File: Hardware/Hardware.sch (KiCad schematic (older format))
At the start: 13 parts

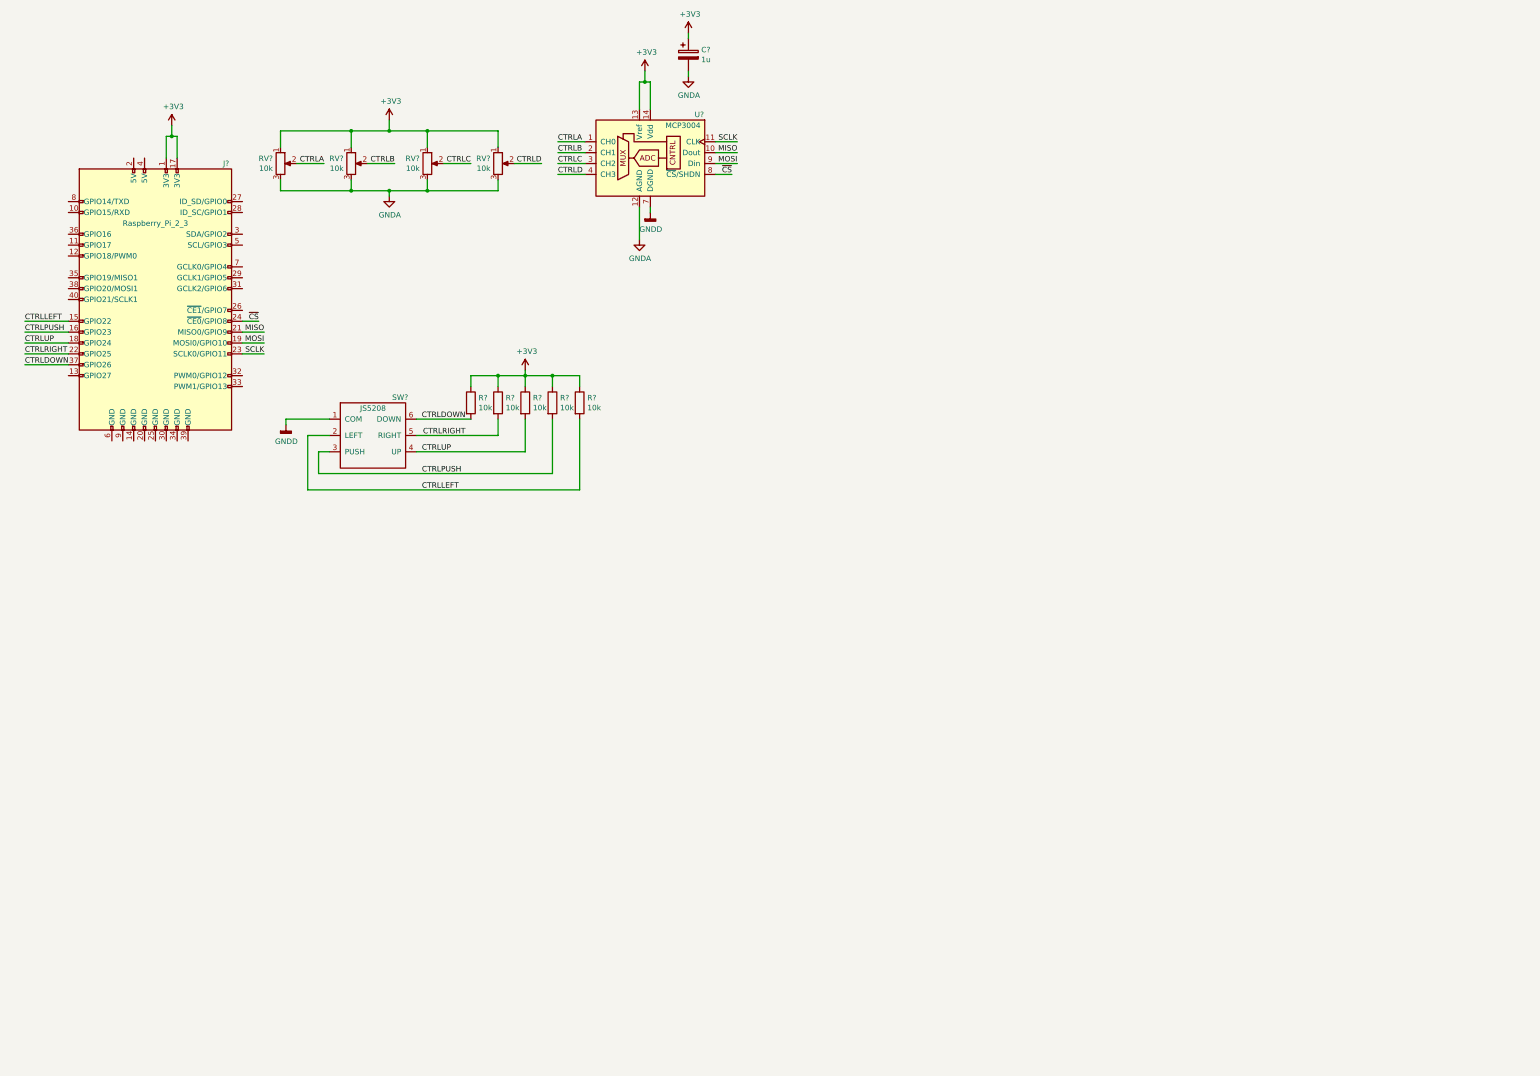
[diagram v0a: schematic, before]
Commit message: Added WM8731SEDS to schematic and connected all relevant external circuitry, modified WM8731SEDS schematic part to aid routing
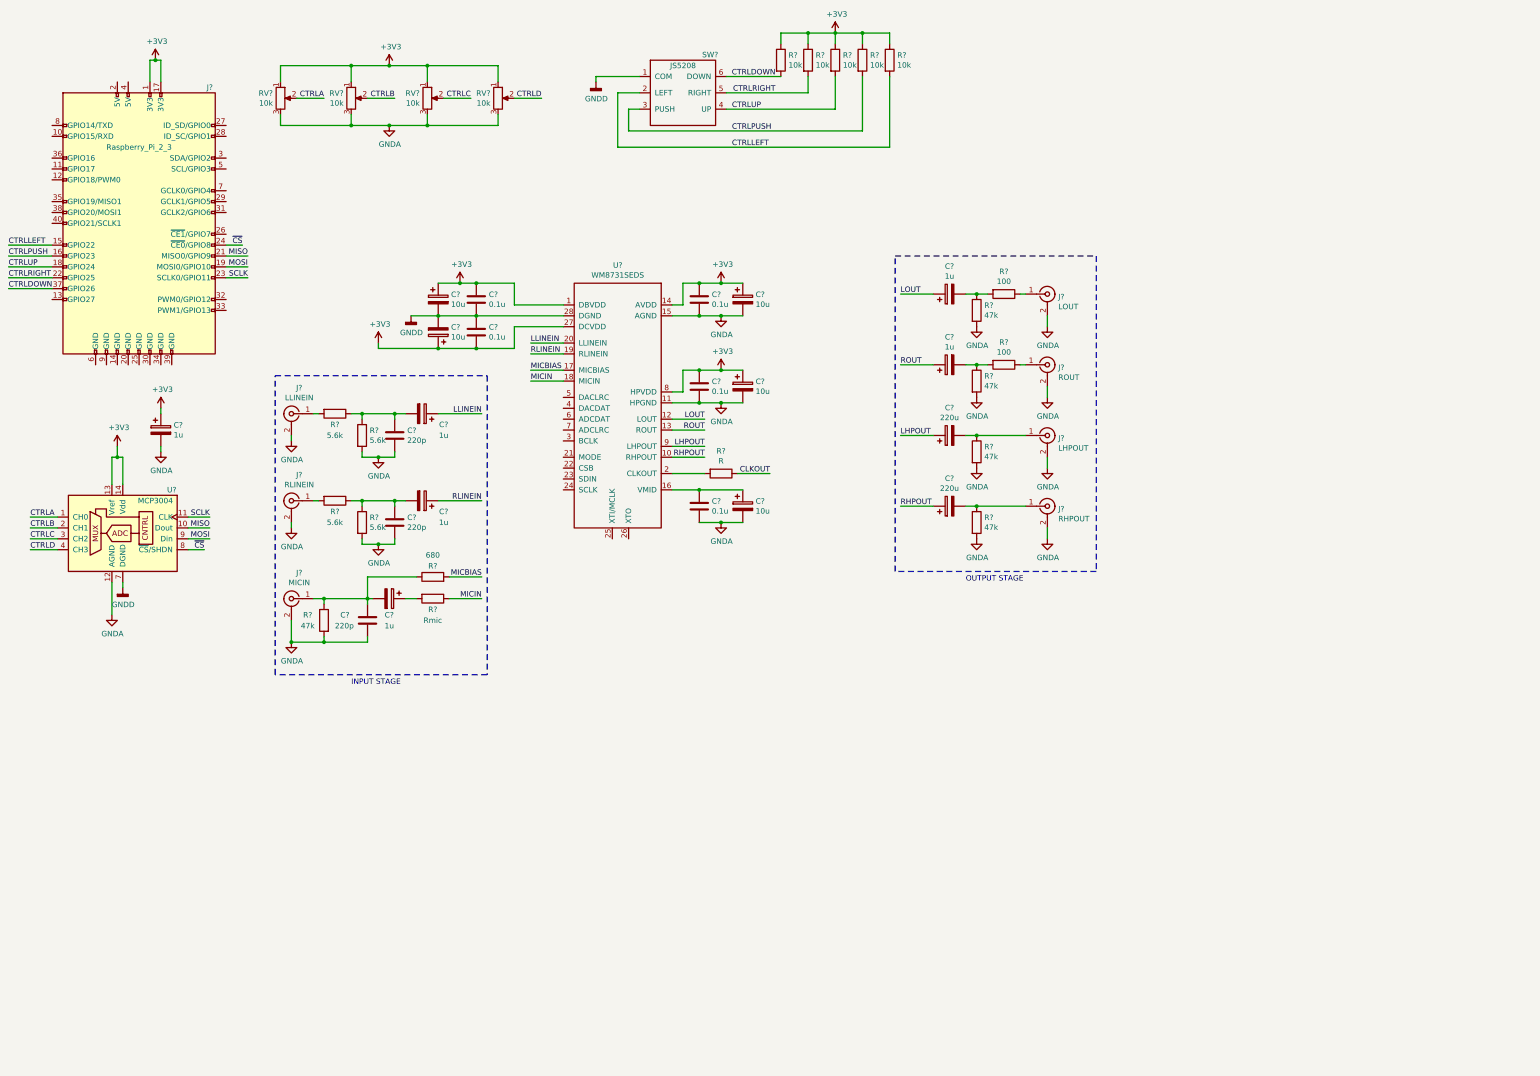
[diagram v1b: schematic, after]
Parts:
- added C? (x5): 0.1u, symbol Device:C
- added C? (x5): 10u, symbol Device:CP
- added C? (x5): 1u, symbol Device:CP
- added C? (x3): 220p, symbol Device:C
- added C? (x2): 220u, symbol Device:CP
- added J?: LLINEIN, symbol Connector:Conn_Coaxial
- added J?: RLINEIN, symbol Connector:Conn_Coaxial
- added J?: MICIN, symbol Connector:Conn_Coaxial
- added J?: LOUT, symbol Connector:Conn_Coaxial
- added J?: ROUT, symbol Connector:Conn_Coaxial
- added J?: LHPOUT, symbol Connector:Conn_Coaxial
- added J?: RHPOUT, symbol Connector:Conn_Coaxial
- added R? (x4): 5.6k, symbol Device:R
- added R?: 680, symbol Device:R
- added R?: Rmic, symbol Device:R
- added R? (x5): 47k, symbol Device:R
- added R? (x2): 100, symbol Device:R
- added R?: R, symbol Device:R
- added U?: WM8731SEDS, Package_SO:SSOP-28_5.3x10.2mm_P0.65mm, symbol signl:WM8731SEDS
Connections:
- net +3V3: now also C?.1, C?.1, C?.1, C?.1, C?.1, C?.1, C?.1, C?.2, U?.1 (DBVDD), U?.14 (AVDD), U?.27 (DCVDD), U?.8 (HPVDD)
- net GNDA: now also C?.2, C?.2, C?.2, C?.2, C?.2, C?.2, C?.2, C?.2, C?.2, J?.2 (Ext), J?.2 (Ext), J?.2 (Ext), J?.2 (Ext), J?.2 (Ext), J?.2 (Ext), J?.2 (Ext), R?.2, R?.2, R?.2, R?.2, R?.2, R?.2, R?.2, U?.11 (HPGND), U?.15 (AGND)
- net GNDD: now also C?.1, C?.2, C?.2, C?.2, U?.28 (DGND)
- new net: C?.1, C?.1, U?.16 (VMID)
- new net: R?.2, U?.2 (CLKOUT)
- new net: C?.1, C?.2, R?.1, R?.1 (x2)
- new net: J?.1 (In), R?.2 (x2)
- new net: C?.1, C?.2, J?.1 (In), R?.1, R?.1
- new net: C?.1, R?.2
- new net: C?.2, R?.1, R?.2 (x2)
- new net: J?.1 (In), R?.1 (x2)
- new net: C?.2, J?.1 (In), R?.1 (x2)
- new net CLKOUT: R?.1
- new net LHPOUT: C?.1, U?.9 (LHPOUT)
- new net LLINEIN: C?.1, U?.20 (LLINEIN)
- new net LOUT: C?.1, U?.12 (LOUT)
- new net MICBIAS: R?.2, U?.17 (MICBIAS)
- new net MICIN: R?.1, U?.18 (MICIN)
- new net RHPOUT: C?.1, U?.10 (RHPOUT)
- new net RLINEIN: C?.1, U?.19 (RLINEIN)
- new net ROUT: C?.1, U?.13 (ROUT)
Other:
- note added: "INPUT STAGE"
- note added: "OUTPUT STAGE"
- moved on the sheet: C?, J?, R?, RV?, SW?, U?

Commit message: Connected WM8731SEDS audio codec to Raspberry Pi through I2S
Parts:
- removed R?: Rmic, symbol Device:R
- added RV?: R_POT, symbol Device:R_POT
- J?: footprint (none) -> Connector_PinHeader_2.54mm:PinHeader_2x20_P2.54mm_Vertical
- R?: value R -> 100
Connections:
- net MICIN: now also RV?.3
- net BCLK: now reaches J?.12 (GPIO18/PWM0)
- net BCLK: now also U?.3 (BCLK)
- net LRC: now reaches J?.35 (GPIO19/MISO1)
- net LRC: now also U?.5 (DACLRC), U?.7 (ADCLRC)
- net ADCDAT: now reaches J?.38 (GPIO20/MOSI1)
- net ADCDAT: now also U?.6 (ADCDAT)
- net DACDAT: now reaches J?.40 (GPIO21/SCLK1)
- net DACDAT: now also U?.4 (DACDAT)
- net at C?.1: now also RV?.2
- no-connect marks 0 -> 3
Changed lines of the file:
@@
 EELAYER 30 0
 EELAYER END
-$Descr A4 11693 8268
+$Descr A3 16535 11693
 encoding utf-8
 Sheet 1 1
@@
 F 0 "J?" H 2650 3850 50  0000 C CNN
 F 1 "Raspberry_Pi_2_3" H 2000 3300 50  0000 C CNN
-F 2 "" H 2000 2600 50  0001 C CNN
+F 2 "Connector_PinHeader_2.54mm:PinHeader_2x20_P2.54mm_Vertical" H 2000 2600 50  0001 C CNN
 F 3 "https://www.raspberrypi.org/documentation/hardware/raspberrypi/schematics/rpi_SCH_3bplus_1p0_reduced.pdf" H 2000 2600 50  0001 C CNN
 	1    2000 2600
@@
 U 1 1 5E4A86BA
 P 4600 4350
-F 0 "C?" V 4500 4550 50  0000 C CNN
-F 1 "1u" V 4400 4550 50  0000 C CNN
+F 0 "C?" V 4850 4350 50  0000 C CNN
+F 1 "1u" V 4750 4350 50  0000 C CNN
 F 2 "" H 4638 4200 50  0001 C CNN
 F 3 "~" H 4600 4350 50  0001 C CNN
@@
 U 1 1 5E4B5C73
 P 4350 4550
-F 0 "C?" H 4465 4596 50  0000 L CNN
-F 1 "220p" H 4465 4505 50  0000 L CNN
+F 0 "C?" H 4450 4600 50  0000 L CNN
+F 1 "220p" H 4450 4500 50  0000 L CNN
 F 2 "" H 4388 4400 50  0001 C CNN
 F 3 "~" H 4350 4550 50  0001 C CNN
@@
 U 1 1 5E4B664C
 P 4050 4550
-F 0 "R?" H 4120 4596 50  0000 L CNN
-F 1 "5.6k" H 4120 4505 50  0000 L CNN
+F 0 "R?" H 4100 4600 50  0000 L CNN
+F 1 "5.6k" H 4100 4500 50  0000 L CNN
 F 2 "" V 3980 4550 50  0001 C CNN
 F 3 "~" H 4050 4550 50  0001 C CNN
@@
 U 1 1 5E4F190B
 P 4050 5350
-F 0 "R?" H 4120 5396 50  0000 L CNN
-F 1 "5.6k" H 4120 5305 50  0000 L CNN
+F 0 "R?" H 4100 5400 50  0000 L CNN
+F 1 "5.6k" H 4100 5300 50  0000 L CNN
 F 2 "" V 3980 5350 50  0001 C CNN
 F 3 "~" H 4050 5350 50  0001 C CNN
@@
 $EndComp
 $Comp
-L Device:R R?
-U 1 1 5E4FD37A
-P 4700 6050
-F 0 "R?" V 4800 6050 50  0000 C CNN
-F 1 "Rmic" V 4900 6050 50  0000 C CNN
-F 2 "" V 4630 6050 50  0001 C CNN
-F 3 "~" H 4700 6050 50  0001 C CNN
-	1    4700 6050
-	0    1    1    0
-$EndComp
-$Comp
 L Device:CP C?
 U 1 1 5E50C9FA
@@
 P 7350 4900
 F 0 "R?" V 7143 4900 50  0000 C CNN
-F 1 "R" V 7234 4900 50  0000 C CNN
+F 1 "100" V 7234 4900 50  0000 C CNN
 F 2 "" V 7280 4900 50  0001 C CNN
 F 3 "~" H 7350 4900 50  0001 C CNN
@@
 Text Notes 3950 6850 0    50   ~ 0
 INPUT STAGE
+Text Label 800  2200 0    50   ~ 0
+BCLK
+Wire Wire Line
+	800  2200 1200 2200
+Text Label 800  2600 0    50   ~ 0
+DACDAT
+Wire Wire Line
+	800  2600 1200 2600
+Text Label 800  2400 0    50   ~ 0
+LRC
+Wire Wire Line
+	800  2400 1200 2400
+Text Label 800  2500 0    50   ~ 0
+ADCDAT
+Wire Wire Line
+	800  2500 1200 2500
+Text Label 5600 4600 0    50   ~ 0
+BCLK
+Wire Wire Line
+	5600 4600 5900 4600
+Text Label 5600 4500 0    50   ~ 0
+LRC
+Wire Wire Line
+	5600 4500 5900 4500
+Text Label 5600 4200 0    50   ~ 0
+LRC
+Wire Wire Line
+	5600 4200 5900 4200
+Text Label 5600 4400 0    50   ~ 0
+ADCDAT
+Wire Wire Line
+	5600 4400 5900 4400
+Text Label 5600 4300 0    50   ~ 0
+DACDAT
+Wire Wire Line
+	5600 4300 5900 4300
+$Comp
+L Device:R_POT RV?
+U 1 1 5E50B9EA
+P 4850 6200
+F 0 "RV?" H 4780 6154 50  0000 R CNN
+F 1 "R_POT" H 4780 6245 50  0000 R CNN
+F 2 "" H 4850 6200 50  0001 C CNN
+F 3 "~" H 4850 6200 50  0001 C CNN
+	1    4850 6200
+	-1   0    0    1
+$EndComp
+Wire Wire Line
+	4700 6200 4550 6200
+Wire Wire Line
+	4550 6200 4550 6050
+NoConn ~ 4850 6350
+NoConn ~ 6350 5500
+NoConn ~ 6500 5500
 $EndSCHEMATC

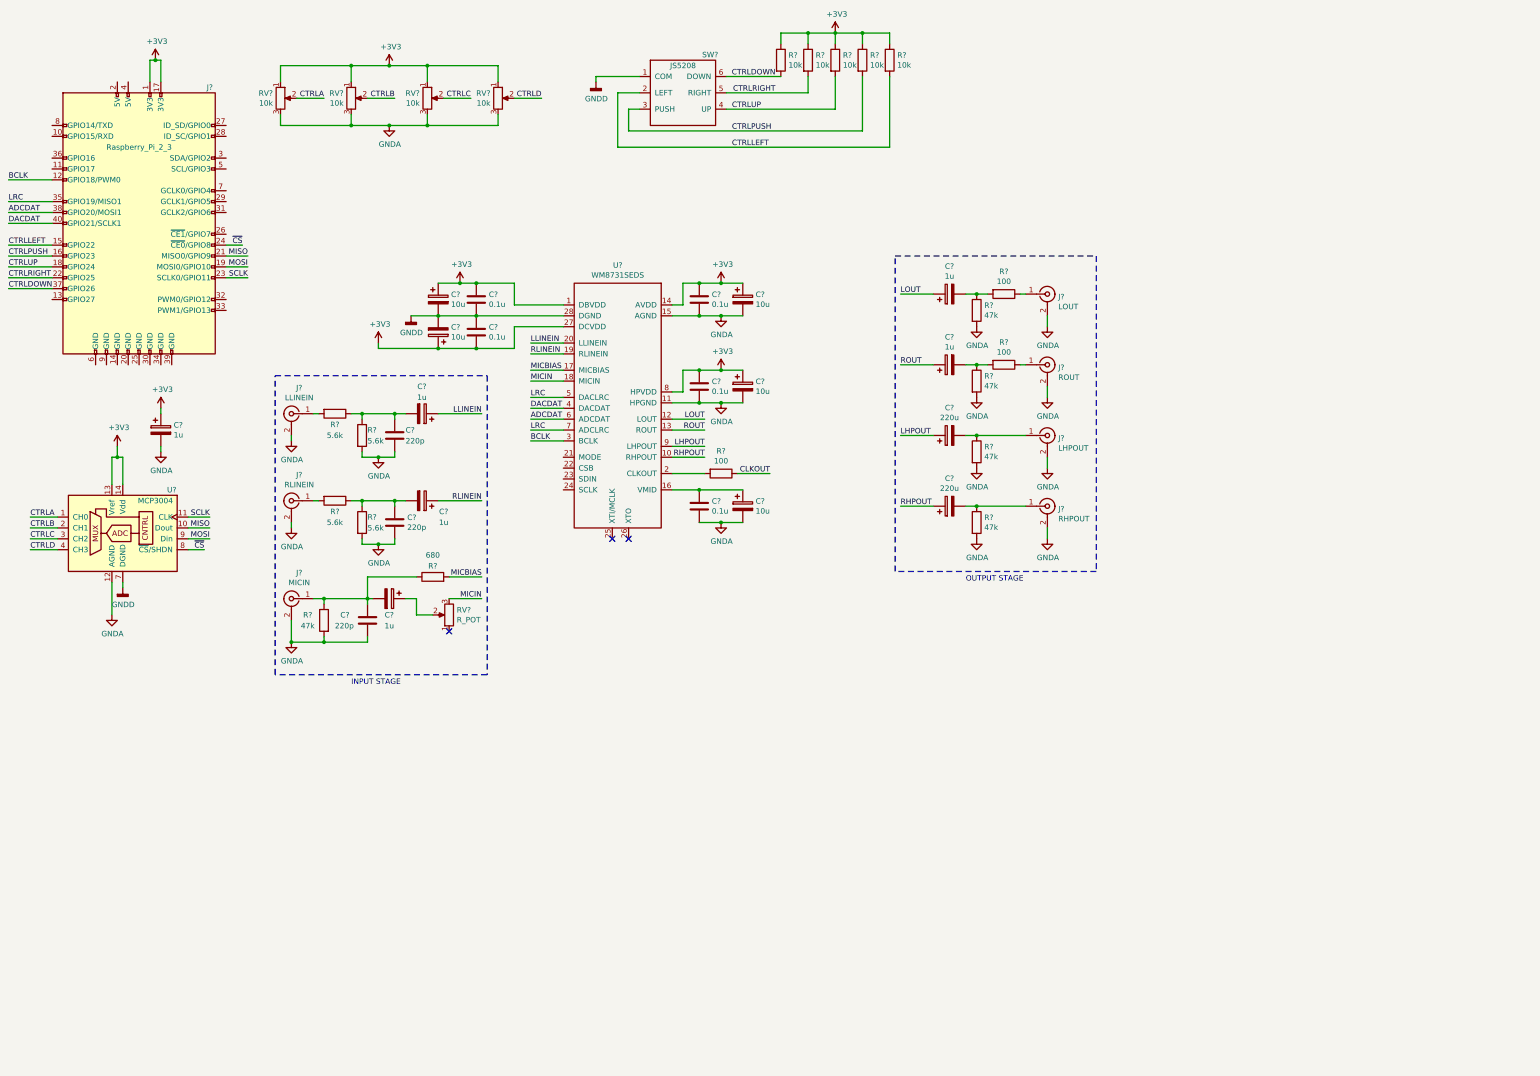
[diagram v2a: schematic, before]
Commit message: Added DOGM128W-6 LCD Screen to schematic with supporting circutiry, corrected error in DOGM128W-6 Schematic part
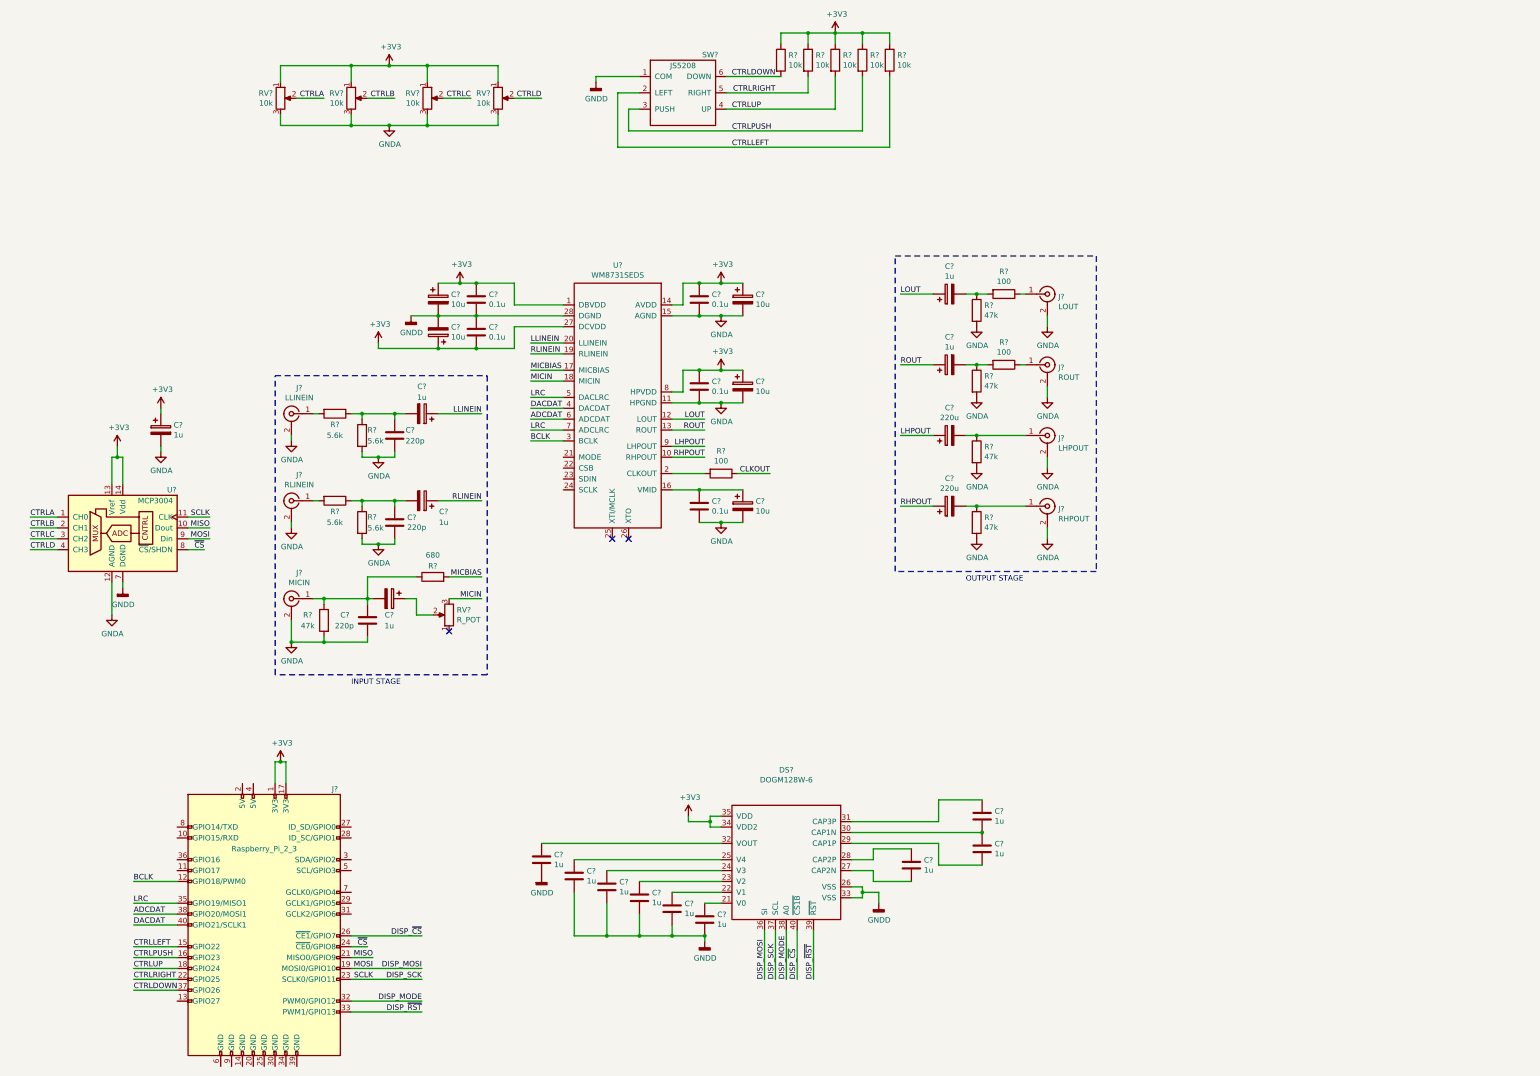
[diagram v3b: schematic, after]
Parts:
- added C? (x9): 1u, symbol Device:C
- added DS?: DOGM128W-6, symbol signl:DOGM128W-6
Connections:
- net +3V3: now also DS?.34 (VDD2), DS?.35 (VDD)
- net GNDD: now also C?.2, C?.2, C?.2, C?.2, C?.2, C?.2, DS?.26 (VSS), DS?.33 (VSS)
- net DISP_~CS~: now reaches J?.26 (~CE1~/GPIO7)
- net DISP_~CS~: now also DS?.40 (~CS1B~)
- net DISP_MODE: now reaches J?.32 (PWM0/GPIO12)
- net DISP_MODE: now also DS?.38 (A0)
- net DISP_~RST~: now reaches J?.33 (PWM1/GPIO13)
- net DISP_~RST~: now also DS?.39 (~RST~)
- net MOSI renamed DISP_MOSI
- net DISP_MOSI: now also DS?.36 (SI)
- net SCLK renamed DISP_SCK
- net DISP_SCK: now also DS?.37 (SCL)
- new net: DS?.1 (A1), DS?.18 (C1), DS?.19 (C2), DS?.2 (A2), DS?.20 (C3), DS?.3 (A3)
- new net: C?.1, DS?.21 (V0)
- new net: C?.1, DS?.22 (V1)
- new net: C?.1, DS?.23 (V2)
- new net: C?.1, DS?.24 (V3)
- new net: C?.1, DS?.25 (V4)
- new net: C?.2, DS?.27 (CAP2N)
- new net: C?.1, DS?.28 (CAP2P)
- new net: C?.2, DS?.29 (CAP1P)
- new net: C?.1, C?.2, DS?.30 (CAP1N)
- new net: C?.1, DS?.31 (CAP3P)
- new net: C?.1, DS?.32 (VOUT)
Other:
- moved on the sheet: J?
